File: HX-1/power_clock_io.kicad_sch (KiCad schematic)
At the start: 32 parts, among them J2 Conn_01x02_Socket, J5 3V3_Out, U3 XC6206P332MR-G, Y1 16MHz

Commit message: Position most of the passive components on pcb
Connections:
- net V_BATT_RAW: now also D5.2 (K); no longer D5.1 (K)
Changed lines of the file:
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@@
+	)
+	(junction
+		(at 62.23 41.91)
+		(diameter 0)
+		(color 0 0 0 0)
 	)
 	(junction
@@
 	)
 	(junction
-		(at 57.15 41.91)
-		(diameter 0)
-		(color 0 0 0 0)
-	)
-	(junction
 		(at 25.4 184.15)
 		(diameter 0)
@@
 	)
 	(no_connect
-		(at 62.23 43.18)
+		(at 57.15 43.18)
 	)
 	(wire
@@
 	(wire
 		(pts
-			(xy 57.15 41.91) (xy 64.77 41.91)
-		)
-		(stroke
-			(width 0)
-			(type default)
-		)
-	)
-	(wire
-		(pts
 			(xy 46.99 100.33) (xy 60.96 100.33)
 		)
@@
 	(wire
 		(pts
+			(xy 62.23 41.91) (xy 64.77 41.91)
+		)
+		(stroke
+			(width 0)
+			(type default)
+		)
+	)
+	(wire
+		(pts
 			(xy 177.8 107.95) (xy 177.8 110.49)
 		)
@@
 	(wire
 		(pts
-			(xy 54.61 41.91) (xy 57.15 41.91)
+			(xy 54.61 41.91) (xy 62.23 41.91)
 		)
 		(stroke
@@
 	(wire
 		(pts
-			(xy 57.15 41.91) (xy 57.15 43.18)
+			(xy 62.23 41.91) (xy 62.23 43.18)
 		)
 		(stroke
@@
 		)
 		(property "Value" "V_BATT"
-			(at 121.92 31.75 0)
-			(effects
-				(font
+			(at 115.57 31.75 0)
+			(effects
+				(font

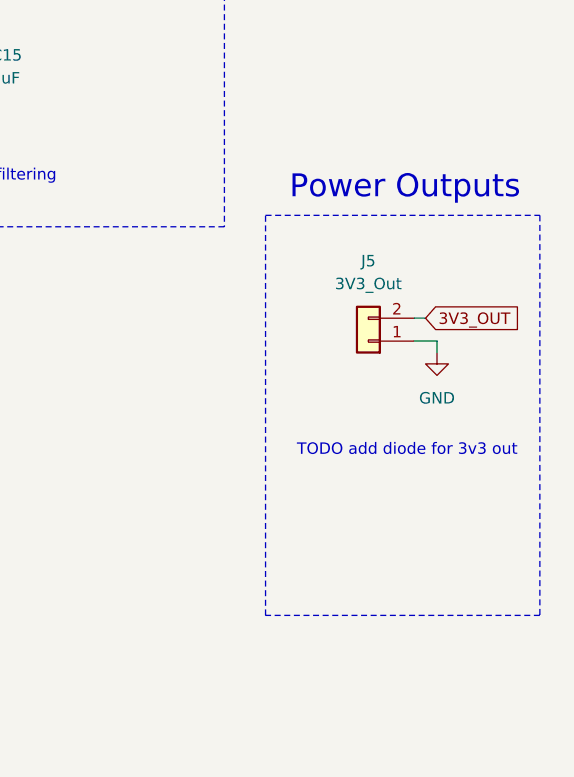
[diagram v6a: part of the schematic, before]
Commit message: remove schematic design for dedicated 3V3 out
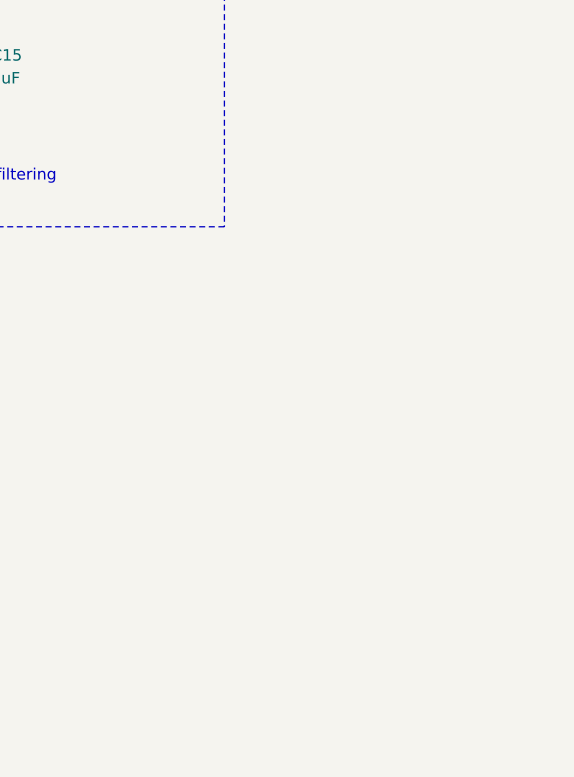
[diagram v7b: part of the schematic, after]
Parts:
- removed J5: 3V3_Out, symbol Connector_Generic:Conn_01x02
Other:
- note removed: "Power Outputs"
- note removed: "TODO add diode for 3v3 out"
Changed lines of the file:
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@@
 	(wire
 		(pts
-			(xy 273.05 133.35) (xy 270.51 133.35)
-		)
-		(stroke
-			(width 0)
-			(type default)
-		)
-	)
-	(wire
-		(pts
 			(xy 21.59 100.33) (xy 34.29 100.33)
 		)
@@
 	(wire
 		(pts
-			(xy 270.51 130.81) (xy 271.78 130.81)
-		)
-		(stroke
-			(width 0)
-			(type default)
-		)
-	)
-	(wire
-		(pts
 			(xy 87.63 107.95) (xy 100.33 107.95)
 		)
@@
 	(wire
 		(pts
-			(xy 273.05 134.62) (xy 273.05 133.35)
-		)
-		(stroke
-			(width 0)
-			(type default)
-		)
-	)
-	(wire
-		(pts
 			(xy 62.23 41.91) (xy 62.23 43.18)
 		)
@@
 	)
 	(rectangle
-		(start 254 119.38)
-		(end 284.48 163.83)
-		(stroke
-			(width 0)
-			(type dash)
-		)
-		(fill
-			(type none)
-		)
-	)
-	(rectangle
 		(start 16.51 20.955)
 		(end 96.52 75.565)
@@
 		)
 	)
-	(text "TODO add diode for 3v3 out"
-		(exclude_from_sim no)
-		(at 269.748 145.542 0)
-		(effects
-			(font
-				(size 1.27 1.27)
-			)
-		)
-	)
 	(text "BATTERY INPUT"
 		(exclude_from_sim no)
@@
 		)
 	)
-	(text "Power Outputs"
-		(exclude_from_sim no)
-		(at 269.494 116.332 0)
-		(effects
-			(font
-				(size 2.54 2.54)
-			)
-		)
-	)
 	(label "3V3_LED"
 		(at 167.64 67.31 180)
@@
 		)
 	)
-	(global_label "3V3_OUT"
-		(shape input)
-		(at 271.78 130.81 0)
-		(fields_autoplaced yes)
-		(effects
-			(font
-				(size 1.27 1.27)
-			)
-			(justify left)
-		)
-		(property "Intersheetrefs" "${INTERSHEET_REFS}"
-			(at 282.869 130.81 0)
-			(effects
-				(font
-					(size 1.27 1.27)
-				)
-				(justify left)
-				(hide yes)
-			)
-		)
-	)
 	(symbol
 		(lib_id "power:+3.3V")
@@
 	)
 	(symbol
-		(lib_id "Connector_Generic:Conn_01x02")
-		(at 265.43 133.35 180)
-		(unit 1)
-		(exclude_from_sim no)
-		(in_bom yes)
-		(on_board yes)
-		(dnp no)
-		(fields_autoplaced yes)
-		(property "Reference" "J5"
-			(at 265.43 124.46 0)
-			(effects
-				(font
-					(size 1.27 1.27)
-				)
-			)
-		)
-		(property "Value" "3V3_Out"
-			(at 265.43 127 0)
-			(effects
-				(font
-					(size 1.27 1.27)
-				)
-			)
-		)
-		(property "Footprint" ""
-			(at 265.43 133.35 0)
-			(effects
-				(font
-					(size 1.27 1.27)
-				)
-				(hide yes)
-			)
-		)
-		(property "Datasheet" "~"
-			(at 265.43 133.35 0)
-			(effects
-				(font
-					(size 1.27 1.27)
-				)
-				(hide yes)
-			)
-		)
-		(property "Description" "Generic connector, single row, 01x02, script generated (kicad-library-utils/schlib/autogen/connector/)"
-			(at 265.43 133.35 0)
-			(effects
-				(font
-					(size 1.27 1.27)
-				)
-				(hide yes)
-			)
-		)
-		(pin "1"
-		)
-		(pin "2"
-		)
-		(instances
-			(project "HX-1"
-				(path "/a3219989-2bf1-44ea-9412-fab86edfb39b/3a90d823-0fb3-4447-b918-f2095473f7ca"
-					(reference "J5")
-					(unit 1)
-				)
-			)
-		)
-	)
-	(symbol
 		(lib_id "power:+5V")
 		(at 76.2 39.37 0)
@@
 					(unit 1)
 				)
-			)
-		)
-	)
-	(symbol
-		(lib_id "power:GND")
-		(at 273.05 134.62 0)
-		(unit 1)
-		(exclude_from_sim no)
-		(in_bom yes)
-		(on_board yes)
-		(dnp no)
-		(fields_autoplaced yes)
-		(property "Reference" "#PWR54"
-			(at 273.05 140.97 0)
-			(effects
-				(font
-					(size 1.27 1.27)
-				)
-				(hide yes)
-			)
-		)
-		(property "Value" "GND"
-			(at 273.05 139.7 0)
-			(effects
-				(font
-					(size 1.27 1.27)
-				)
-			)
-		)
-		(property "Footprint" ""
-			(at 273.05 134.62 0)
-			(effects
-				(font
-					(size 1.27 1.27)
-				)
-				(hide yes)
-			)
-		)
-		(property "Datasheet" ""
-			(at 273.05 134.62 0)
-			(effects
-				(font
-					(size 1.27 1.27)
-				)
-				(hide yes)
-			)
-		)
-		(property "Description" "Power symbol creates a global label with name \"GND\" , ground"
-			(at 273.05 134.62 0)
-			(effects
-				(font
-					(size 1.27 1.27)
-				)
-				(hide yes)
-			)
-		)
-		(pin "1"
-		)
-		(instances
-			(project "HX-1"
-				(path "/a3219989-2bf1-44ea-9412-fab86edfb39b/3a90d823-0fb3-4447-b918-f2095473f7ca"
-					(reference "#PWR54")
-					(unit 1)
-				)

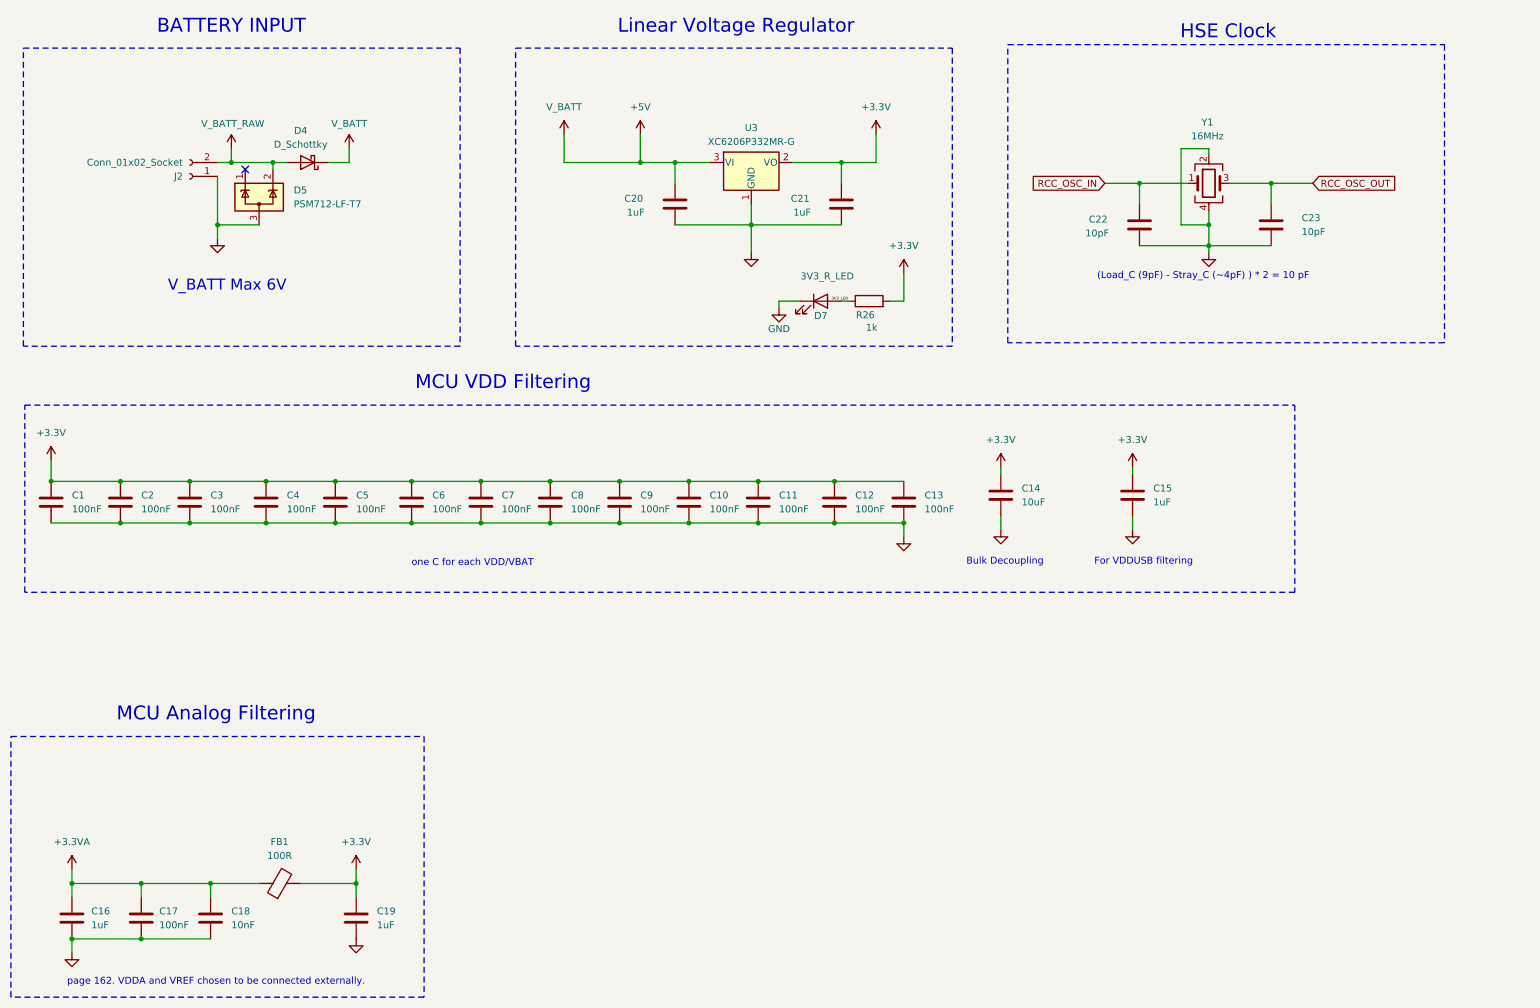
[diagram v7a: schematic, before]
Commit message: tidy up schematics and change groupings on each sheet
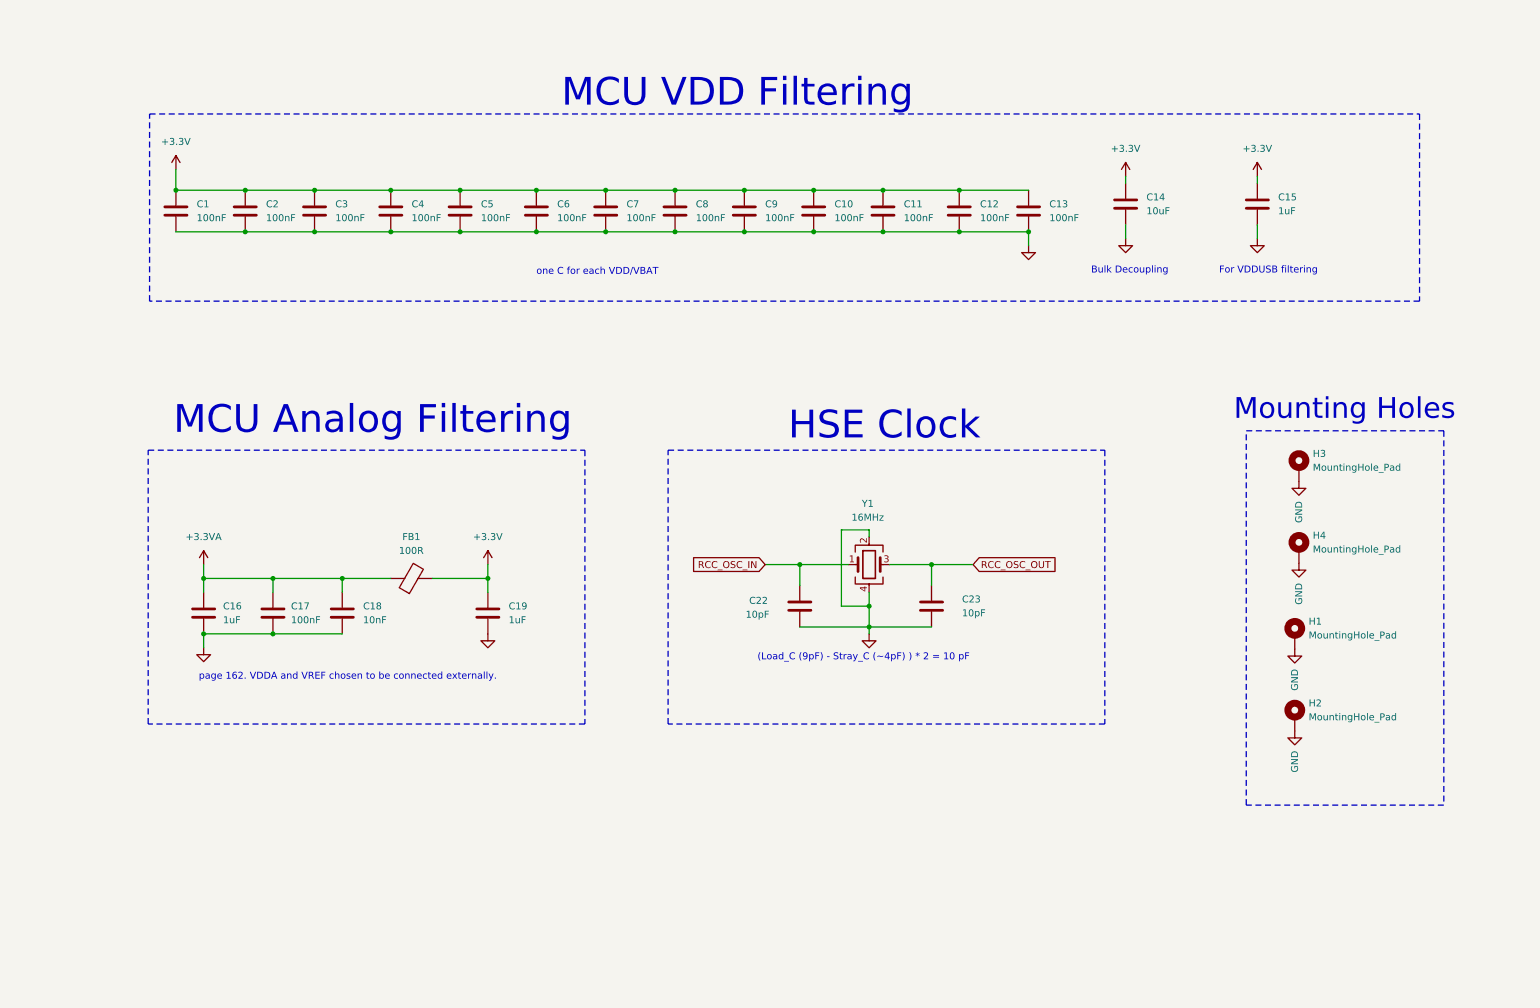
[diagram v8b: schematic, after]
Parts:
- removed C20, C21: 1uF, Capacitor_SMD:C_0402_1005Metric, symbol Device:C
- removed D4: D_Schottky, Diode_SMD:D_SOD-323, symbol Device:D_Schottky
- removed D5: PSM712-LF-T7, Package_TO_SOT_SMD:SOT-23-3, symbol Power_Protection:ESDA5V3L
- removed D7: 3V3_R_LED, LED_SMD:LED_0603_1608Metric, symbol Device:LED
- removed J2: Conn_01x02_Socket, Connector_JST:JST_PH_B2B-PH-K_1x02_P2.00mm_Vertical, symbol Connector:Conn_01x02_Socket
- removed R26: 1k, Resistor_SMD:R_0603_1608Metric, symbol Device:R
- removed U3: XC6206P332MR-G, Package_TO_SOT_SMD:SOT-23-3, symbol Regulator_Linear:XC6206PxxxMR
- added H1, H2, H3, H4: MountingHole_Pad, MountingHole:MountingHole_3.2mm_M3_Pad, symbol Mechanical:MountingHole_Pad
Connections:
- net GND: now also H1.1, H2.1, H3.1, H4.1
- no-connect marks 1 -> 0
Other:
- note added: "Mounting Holes"
- note removed: "BATTERY INPUT"
- note removed: "Linear Voltage Regulator"
- note removed: "V_BATT Max 6V"
- moved on the sheet: C1, C10, C11, C12, C13, C14, C15, C16, C17, C18, C19, C2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
